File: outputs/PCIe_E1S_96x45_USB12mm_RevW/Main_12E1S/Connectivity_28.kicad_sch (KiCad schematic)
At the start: 12 parts

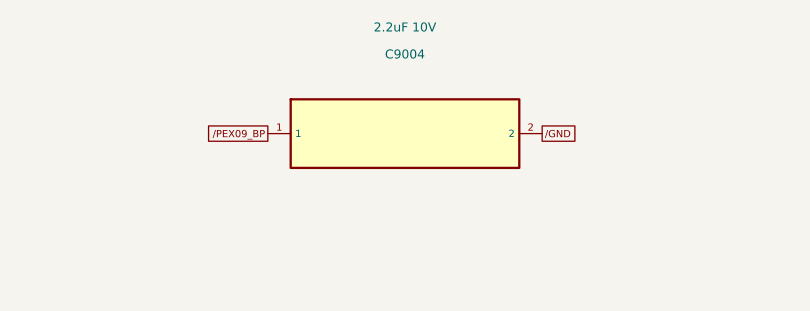
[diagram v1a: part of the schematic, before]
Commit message: Correct E1S BP bypass and support devices; rebuild one PCIe pair
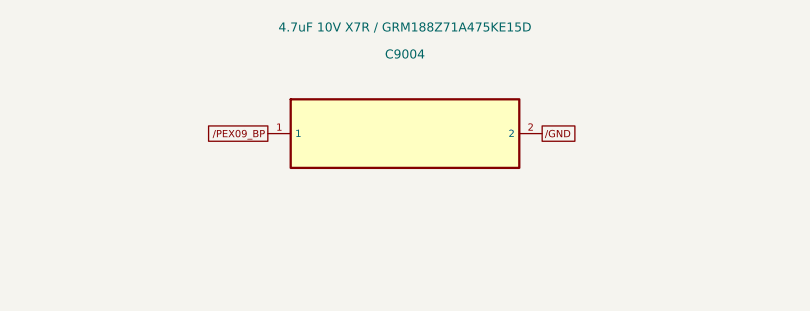
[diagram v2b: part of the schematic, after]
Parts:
- C9004: value 2.2uF 10V -> 4.7uF 10V X7R / GRM188Z71A475KE15D; footprint Local:C_0402_1005Metric -> Local:C_0603_1608Metric_BP_Official
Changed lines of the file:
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@@
 (global_label "/VBANK_B" (shape passive) (at 203.2 73.66 180) (effects (font (size 0.8 0.8)) (justify right)))
 (global_label "/GND" (shape passive) (at 233.68 73.66 0) (effects (font (size 0.8 0.8)) (justify left)))
-(symbol (lib_id "Local:PART_C9004") (at 360.68 73.66 0) (unit 1) (in_bom yes) (on_board yes) (dnp no) (property "Reference" "C9004" (at 360.68 64.85 0) (effects (font (size 1 1))))(property "Value" "2.2uF 10V" (at 360.68 61.849999999999994 0) (effects (font (size 1 1))))(property "Footprint" "Local:C_0402_1005Metric" (at 360.68 73.66 0) (effects (font (size 1 1)) (hide yes)))(pin "1")(pin "2")(instances (project "Main_12E1S" (path "/c33a6c5d-1a9e-4453-a37d-d3058a6ae0e3/23d4ea4f-2c7c-4e89-ab30-3b8b04fe61e1" (reference "C9004") (unit 1)))))
+(symbol (lib_id "Local:PART_C9004") (at 360.68 73.66 0) (unit 1) (in_bom yes) (on_board yes) (dnp no) (property "Reference" "C9004" (at 360.68 64.85 0) (effects (font (size 1 1))))(property "Value" "4.7uF 10V X7R / GRM188Z71A475KE15D" (at 360.68 61.849999999999994 0) (effects (font (size 1 1))))(property "Footprint" "Local:C_0603_1608Metric_BP_Official" (at 360.68 73.66 0) (effects (font (size 1 1)) (hide yes)))(pin "1")(pin "2")(instances (project "Main_12E1S" (path "/c33a6c5d-1a9e-4453-a37d-d3058a6ae0e3/23d4ea4f-2c7c-4e89-ab30-3b8b04fe61e1" (reference "C9004") (unit 1)))))
 (global_label "/PEX09_BP" (shape passive) (at 345.44 73.66 180) (effects (font (size 0.8 0.8)) (justify right)))
 (global_label "/GND" (shape passive) (at 375.92 73.66 0) (effects (font (size 0.8 0.8)) (justify left)))
